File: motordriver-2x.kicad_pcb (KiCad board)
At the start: 4 copper layers, 215 x 130 mm, 651 parts, among them J1 USB_B_Micro, J2 CONN_RJ45_MAG, J3 CONN_RJ45_MAG, P1 CONN_BUTTON, P11 CONN_JOYSTICK, P13 CONN_SENSOR, P14 CONN_SENSOR, P15 CONN_SENSOR, P16 CONN_SENSOR, P17 CONN_DEBUG_2R, P18 CONN_POWER_41A, P19 CONN_CAN, P2 CONN_BUTTON, P20 CONN_CAN, P21 CONN_AN_OUT, P22 CONN_AN_OUT, P23 CONN_POWER_10A, P24 CONN_CAN, P25 CONN_LCD, P26 CONN_AN_OUT, P27 CONN_AN_OUT, P28 CONN_UEXT, P3 CONN_BUTTON, P37 CONN_ENCODER, P38 CONN_SENSOR, P39 CONN_SENSOR, P4 CONN_BUTTON, P40 CONN_SENSOR, P41 CONN_ENCODER, P42 CONN_SENSOR, P43 CONN_SENSOR, P44 CONN_SENSOR, P45 CONN_MOTOR, P46 CONN_MOTOR, P47 CONN_HALL, P48 CONN_HALL, P49 CONN_BRKRES, P5 CONN_BUTTON, P6 CONN_BUTTON, P7 CONN_BUTTON, P8 CONN_BUTTON, P9 CONN_JOYSTICK, Q1 Q_NMOS_2X_60V_63A, Q2 Q_NMOS_2X_60V_63A, Q3 Q_NMOS_2X_60V_63A, Q4 Q_NMOS_2X_60V_63A, Q5 Q_NMOS_2X_60V_63A, Q6 Q_NMOS_2X_60V_63A, Q7 Q_PNP_BC856, Q8 Q_NMOS_BUK9875, U1 IC_MIC2026, U10 IC_MCP4461, U11 IC_MCP2517FD-xJHA, U12 IC_STM32F429ZET6, U13 IC_MCP23S17, U14 IC_TPS54360DDA, U15 IC_TJA1044GT3, U16 IC_TLV2474, U17 IC_M24C16, U18 IC_USBLC6-2, U19 IC_TPS62147RGXR, U2 IC_MAX6818, U20 IC_TLV75533, U21 IC_LP55231, U22 IC_TLV75533, U23 IC_MAX14890, U24 IC_MAX14890, U25 IC_MIC2026, U26 IC_TLV2474, U27 IC_USBLC6-2, U28 IC_USBLC6-2, U29 IC_MCP4461, U3 IC_TLV2474, U30 IC_LAN9252, U31 IC_DRV8302, U32 IC_DRV8302, U33 IC_TLV2474, U34 IC_M24C16, U35 IC_TLV2474, U36 IC_TLV75533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

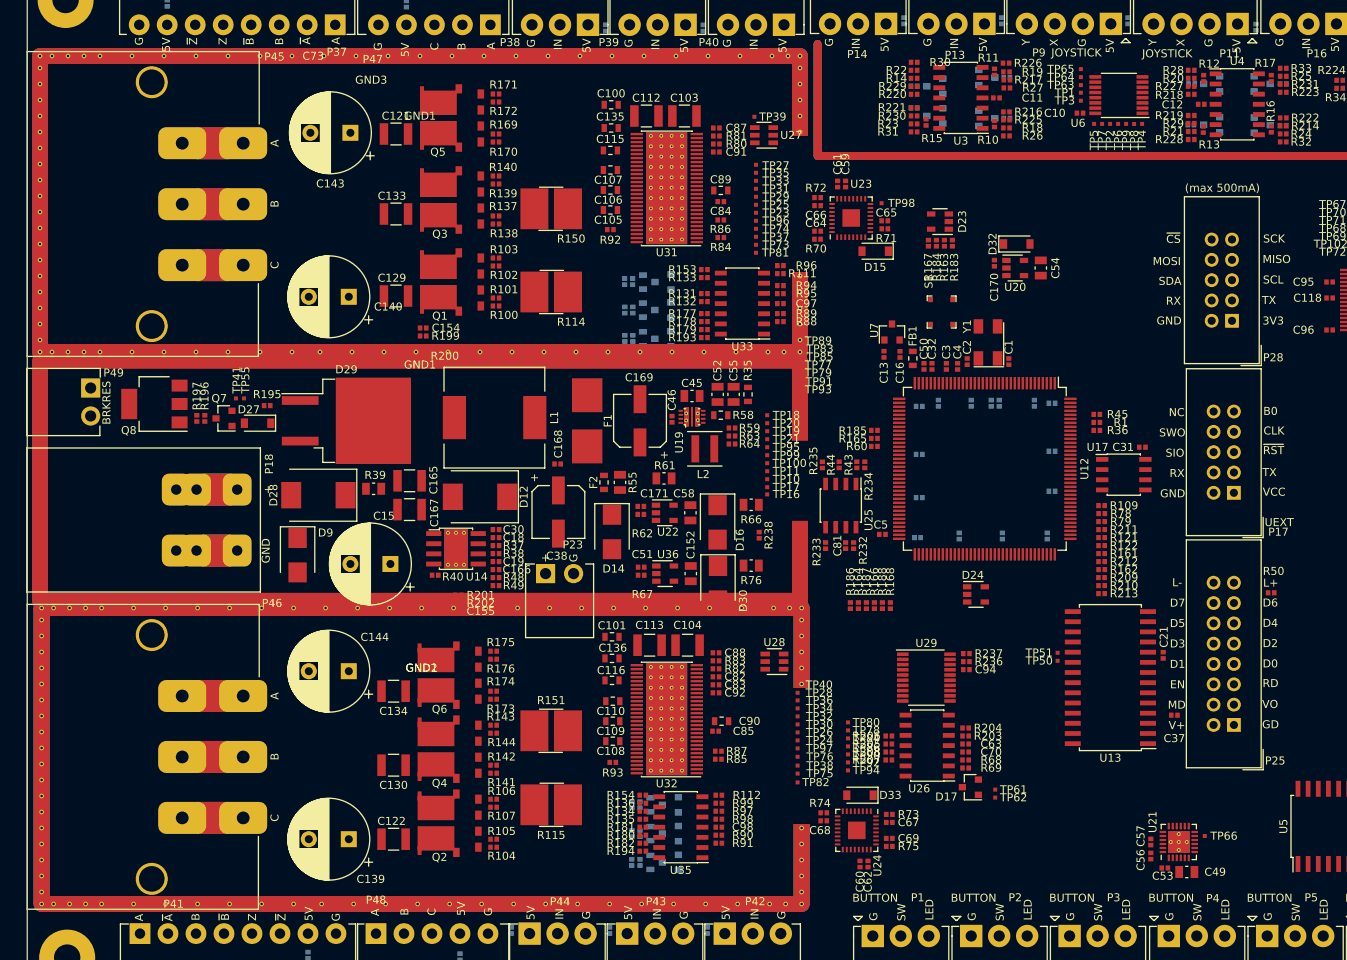
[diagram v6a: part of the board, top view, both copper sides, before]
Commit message: update grounds and connectors
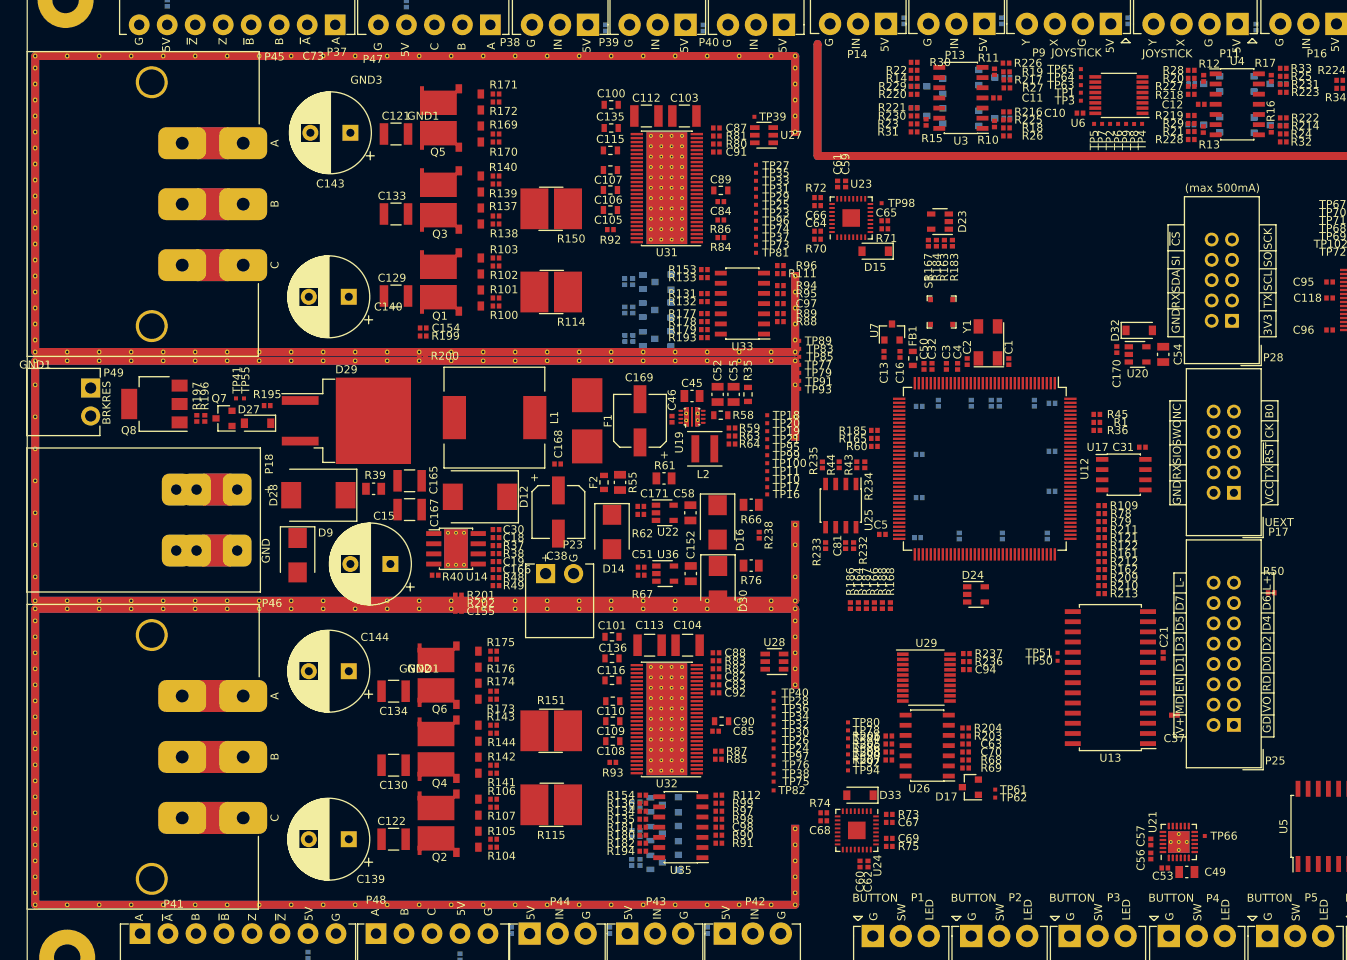
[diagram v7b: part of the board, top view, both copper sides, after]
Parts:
- moved GND1 48.1 mm to (47.0, 74.2)
- moved C54 18.7 mm to (188.0, 73.4)
- moved D32 18.7 mm to (185.0, 70.4)
- moved U20 18.7 mm to (184.8, 73.4)
- moved C170 18.7 mm to (182.2, 72.8)
- moved TP24 3.16 mm to (139.3, 122.7)
- moved TP26 3.16 mm to (139.3, 121.7)
- moved TP28 3.16 mm to (139.3, 116.7)
- moved TP30 3.16 mm to (139.3, 120.7)
- moved TP32 3.16 mm to (139.3, 119.7)
- moved TP34 3.16 mm to (139.3, 118.7)
- moved TP36 3.16 mm to (139.3, 117.7)
- moved TP38 3.16 mm to (139.3, 125.8)
- moved TP40 3.16 mm to (139.3, 115.7)
- moved TP75 3.16 mm to (139.3, 126.8)
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
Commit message: start routing
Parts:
- moved D16 2.40 mm to (132.3, 92.0)
- moved D30 2.40 mm to (132.3, 99.6)
- moved C123 2.02 mm to (124.1, 62.7)
- moved D19 2.02 mm to (126.6, 62.7)
- moved R117 2.02 mm to (122.8, 62.6)
- moved R118 2.02 mm to (121.8, 62.6)
- moved C145 2.02 mm to (124.1, 66.2)
- moved C149 2.02 mm to (124.1, 69.8)
- moved D21 2.02 mm to (126.6, 66.2)
- moved D25 2.02 mm to (126.6, 69.8)
- moved R156 2.02 mm to (122.8, 66.2)
- moved R157 2.02 mm to (121.8, 66.2)
- moved R189 2.02 mm to (122.8, 69.7)
- moved R190 2.02 mm to (121.8, 69.7)
- moved C121 0.88 mm to (91.5, 46.5), turned to 270 degrees
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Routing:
- net VMOT: track 0.00 -> 55.2 mm
- net GND: vias 0 -> 11
- added copper zone on B.Cu, net GND
- added copper zone on F.Cu, net GND
- added copper zone on In1.Cu, net GND
- added copper zone on In2.Cu, net GND
- added copper zone on F.Cu, net SLA1
- added copper zone on F.Cu, net SLB1
- added copper zone on F.Cu, net SLC1
- added copper zone on F.Cu, net VMOT_IN
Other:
- net class Default: clearance 0.2 -> 0.152; trace_width 0.25 -> 0.152; via_dia 0.8 -> 0.5; via_drill 0.4 -> 0.2
- rule trace_clearance: 0.2 -> 0.152
- rule trace_min: 0.2 -> 0.152
- rule via_min_drill: 0.3 -> 0.2
- rule via_min_size: 0.4 -> 0.5
- board text added: "0.2mm"
- board text added: "0.75 oz"
- board text added: "1 oz"
- board text added: "1.2mm"
- board text added: "Min trace width/spacing: 6/6mil, 0.152mm Min trace spacing inner layers: 6mil Min spacing trace -> copper: 8mil, 0.2mm Min spacing trace -> np hole: 8mil, 0.2mm Min distance trace -> via: 12mil, 0.34mm Annular ring: 6mil Min solder mask dam: 12mil, 0.34mm Min silkscreen text height: 0.5842mm / 23mil"
